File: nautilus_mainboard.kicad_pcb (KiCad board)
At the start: 4 copper layers, 176.2 x 177.5 mm, 83 parts, among them IC1 STM32H7B0RBT6, IC3 TPS2121RUXT, IC4 TPS2121RUXT, IC5 TPS2121RUXT, J18 179-UJ20CHC4SMTTR, J2 61300211121, J3 1761681-3, J4 Header male 1x05, J5 1792876, J7 LPHT-04-16-L-RT1-GP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

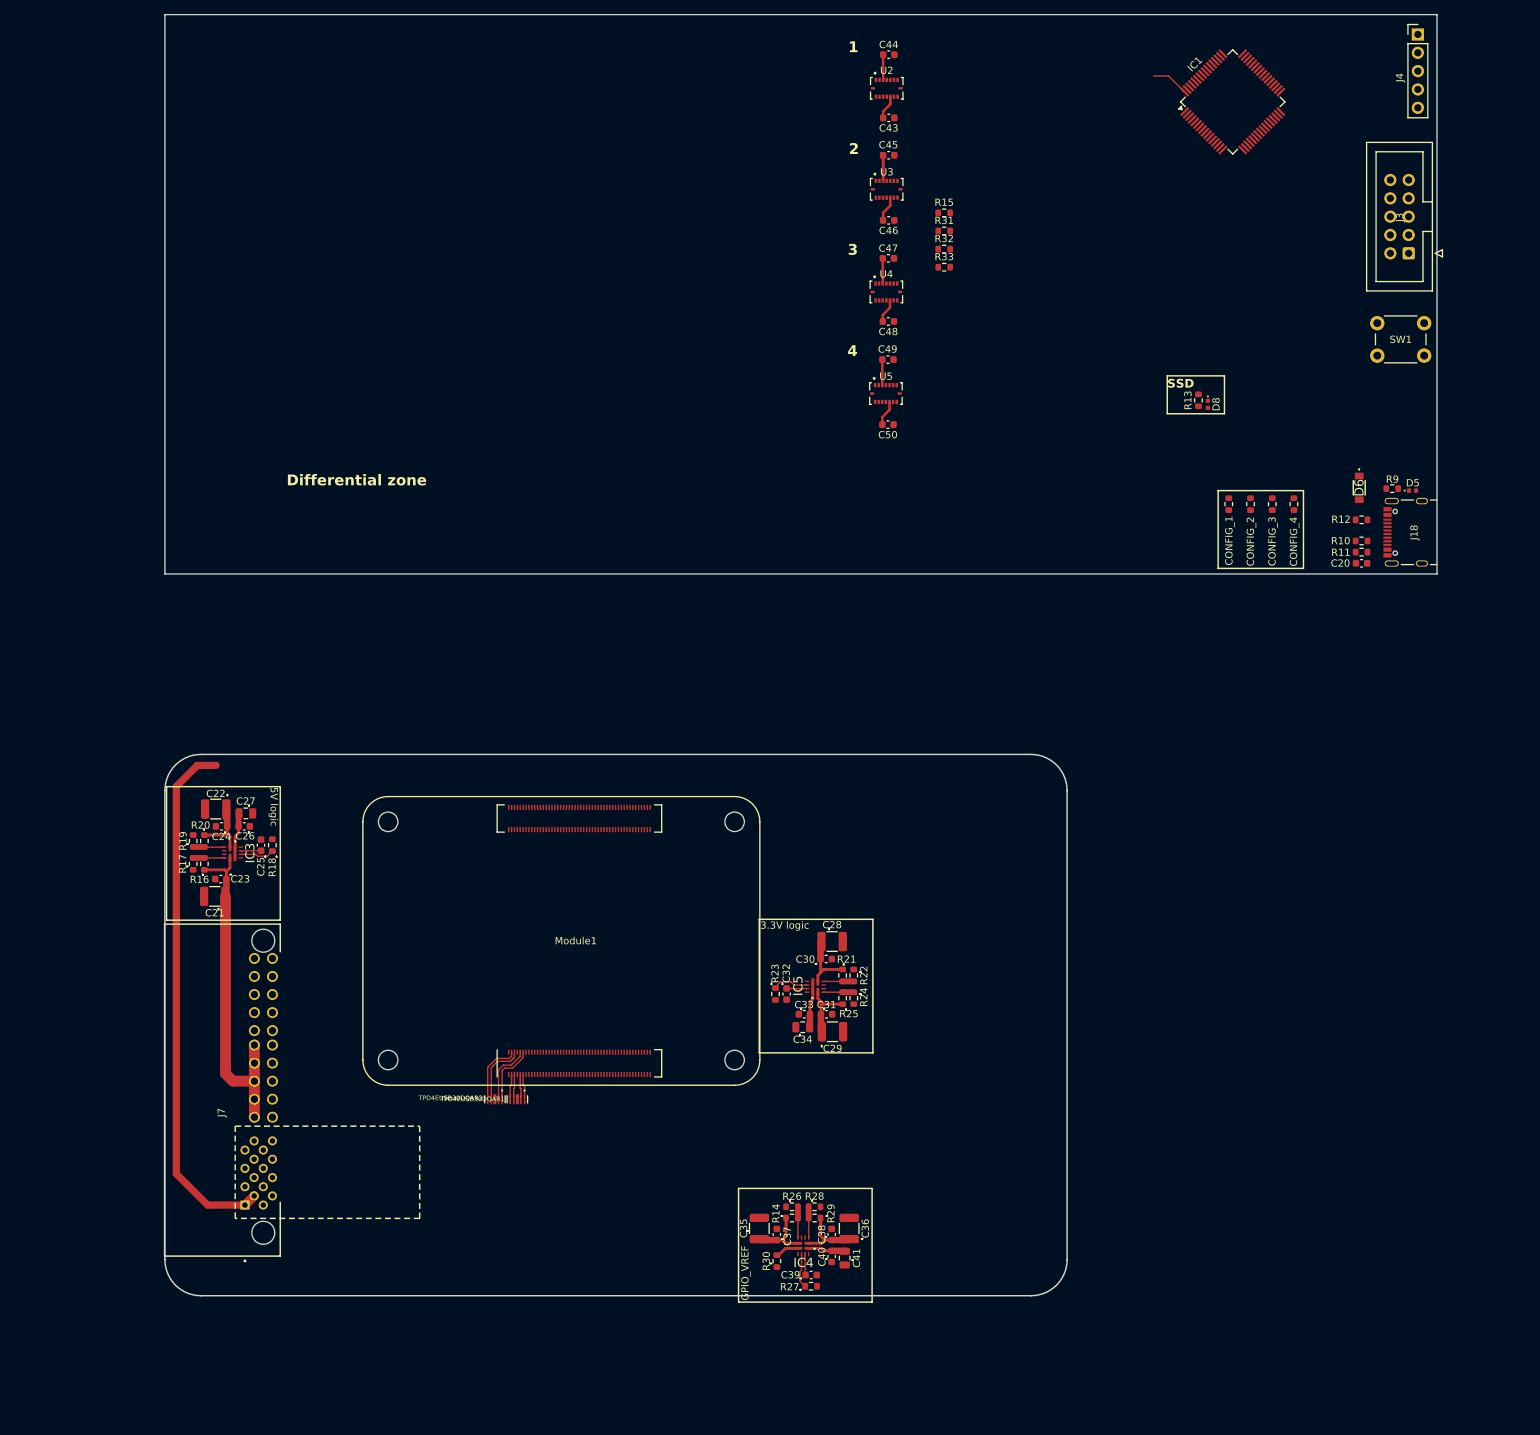
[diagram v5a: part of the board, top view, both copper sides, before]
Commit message: first tries with signal tracks
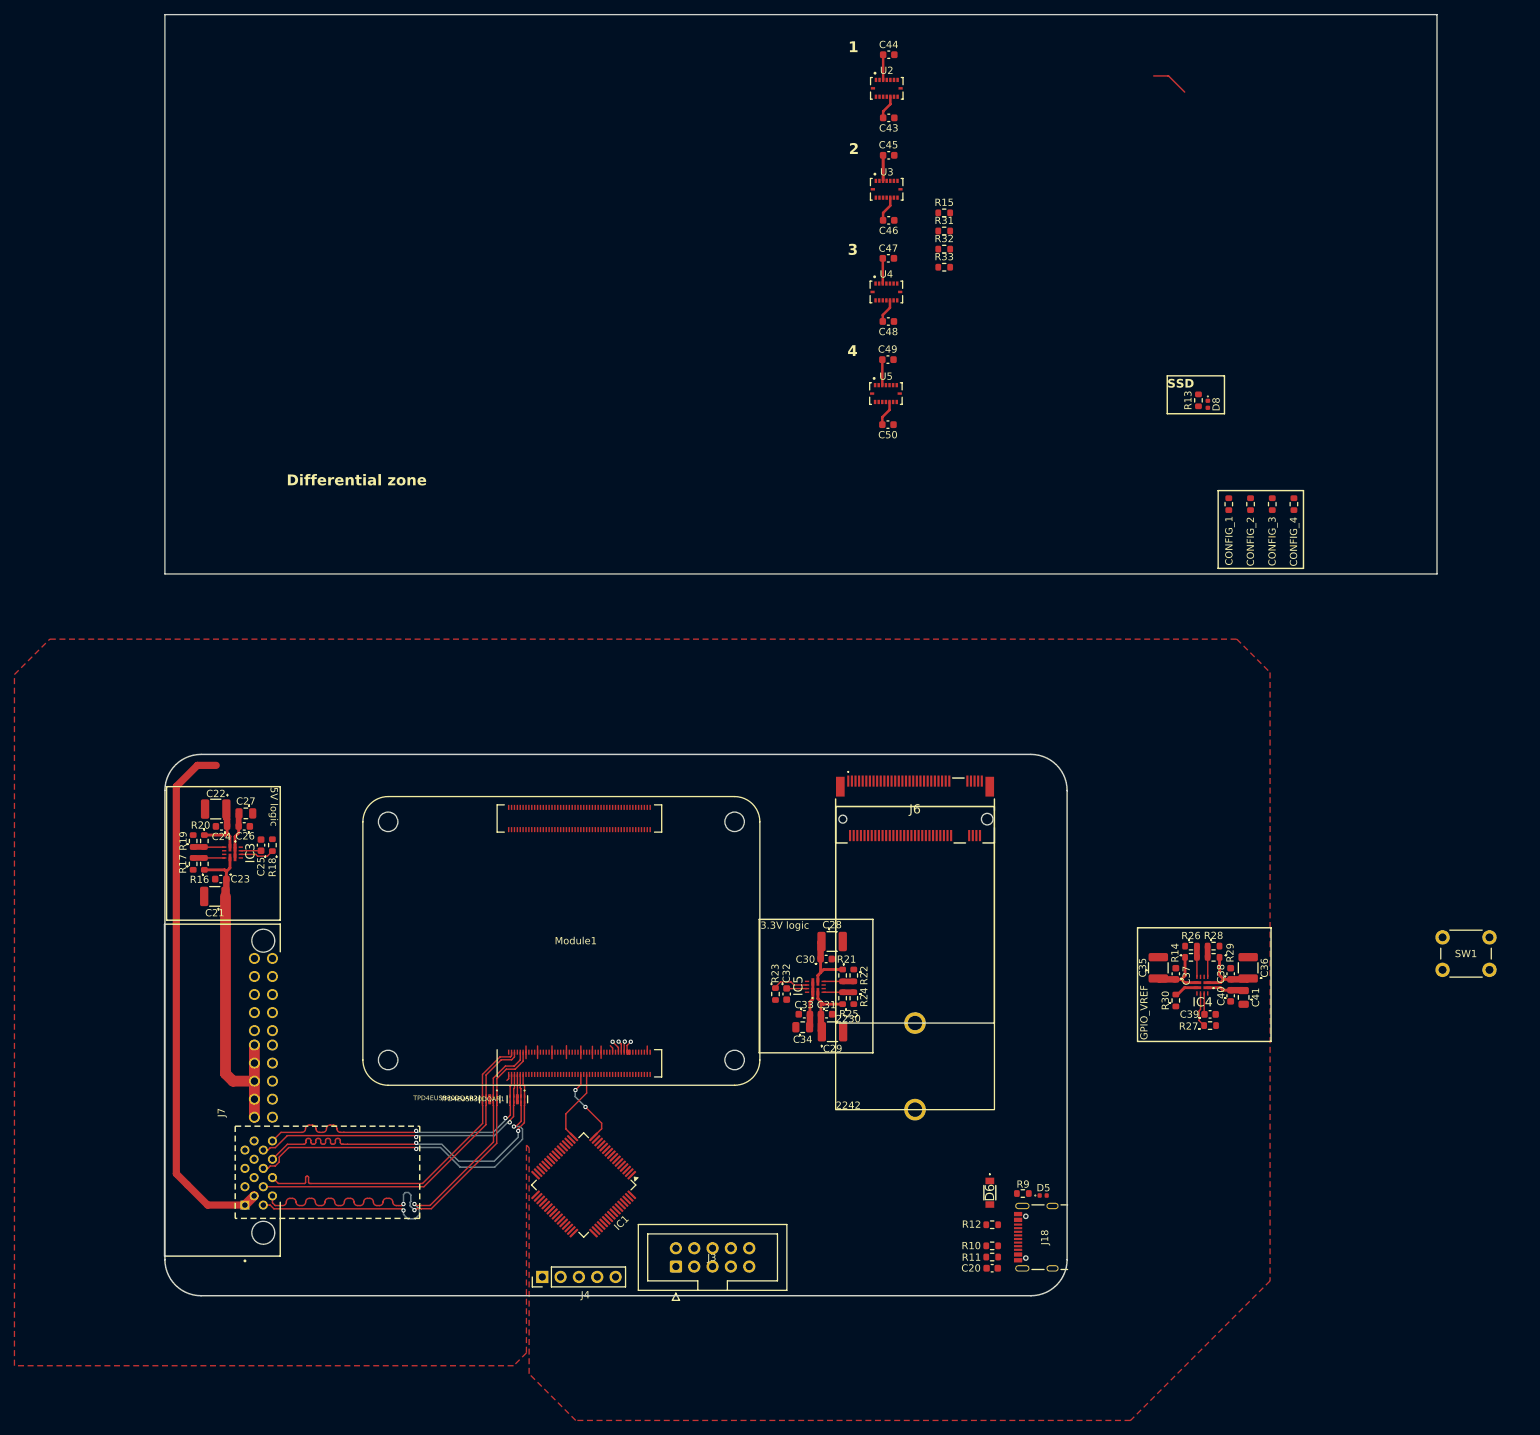
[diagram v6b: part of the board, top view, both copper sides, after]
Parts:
- added J6: MDT275M02001, dz_con:PCIE_MDT275M02001, F.Cu at (174.9, 157.8)
- moved J4 210.6 mm to (123.3, 222.4), turned to 90 degrees
- moved IC1 175.0 mm to (129.0, 209.7), turned to -135 degrees
- moved J3 173.2 mm to (141.8, 221.0), turned to 90 degrees
- moved D5 110.3 mm to (192.7, 211.1)
- moved R10 110.3 mm to (185.6, 218.1)
- moved R9 110.3 mm to (189.9, 210.8)
- moved C20 110.3 mm to (185.6, 221.2)
- moved D6 110.3 mm to (185.3, 210.7)
- moved J18 110.3 mm to (193.0, 216.9)
- moved R11 110.3 mm to (185.6, 219.6)
- moved R12 110.3 mm to (185.6, 215.2)
- moved SW1 85.6 mm to (248.0, 175.3)
- moved C35 66.0 mm to (208.6, 179.6)
- moved C36 66.0 mm to (221.1, 179.6)
- moved C40 66.0 mm to (218.7, 183.4)
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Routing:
- net /CM4/CM4_Module1A/TRD0_P: track 8.78 -> 61.0 mm, vias 0 -> 2
- net /CM4/CM4_Module1A/TRD2_N: track 3.90 -> 51.0 mm, vias 0 -> 2
- net /CM4/CM4_Module1A/TRD2_P: track 3.94 -> 50.9 mm, vias 0 -> 2
- net /CM4/CM4_Module1A/TRD0_N: track 8.83 -> 54.3 mm, vias 0 -> 2
- net /CM4/CM4_Module1A/TRD3_N: track 3.90 -> 42.8 mm, vias 0 -> 2
- net /CM4/CM4_Module1A/TRD3_P: track 3.94 -> 42.6 mm, vias 0 -> 2
- net /CM4/CM4_Module1A/TRD1_P: track 9.35 -> 47.0 mm
- net /CM4/CM4_Module1A/TRD1_N: track 9.52 -> 46.9 mm
- net GND: track 1.67 -> 19.7 mm
- net /CM4/CM4_Module1A/GPIO15: track 0.00 -> 11.0 mm, vias 0 -> 2
- net /CM4/CM4_Module1A/GPIO14: track 0.00 -> 10.3 mm
- net CM4_LED_IN_3.3V: track 9.20 -> 11.3 mm, vias 0 -> 1
- net GPIO_VREF_3.3V: track 8.61 -> 10.4 mm, vias 0 -> 1
- net /CM4/CM4_Module1A/SCL0: track 0.00 -> 1.66 mm, vias 0 -> 1
- net /CM4/CM4_Module1A/SDA0: track 0.00 -> 1.51 mm, vias 0 -> 1
- added copper zone on F.Cu, net GND
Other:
- board text added: "SORRY :("

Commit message: routed the CAN
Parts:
- added C1: 100nF, Capacitor_SMD:C_0603_1608Metric, F.Cu at (276.3, 66.9)
- added C10: 2.2pF, Capacitor_SMD:C_0402_1005Metric, F.Cu at (264.1, 75.9)
- added C11: 100nF, Capacitor_SMD:C_0603_1608Metric, F.Cu at (260.6, 66.9)
- added C12: 10pF, Capacitor_SMD:C_0603_1608Metric, F.Cu at (260.6, 69.4)
- added C13: 10pF, Capacitor_SMD:C_0603_1608Metric, F.Cu at (260.6, 71.9)
- added C14: 10pF, Capacitor_SMD:C_0603_1608Metric, F.Cu at (260.6, 74.4)
- added C15: 2.2pF, Capacitor_SMD:C_0402_1005Metric, F.Cu at (264.1, 77.8)
- added C16: 10pF, Capacitor_SMD:C_0603_1608Metric, F.Cu at (260.6, 76.9)
- added C17: 10pF, Capacitor_SMD:C_0603_1608Metric, F.Cu at (260.6, 79.4)
- added C18: 10pF, Capacitor_SMD:C_0603_1608Metric, F.Cu at (260.6, 81.9)
- added C19: 100nF, Capacitor_SMD:C_0603_1608Metric, F.Cu at (260.6, 84.5)
- added C2: 100nF, Capacitor_SMD:C_0603_1608Metric, F.Cu at (276.3, 69.4)
- added C3: 100nF, Capacitor_SMD:C_0603_1608Metric, F.Cu at (276.3, 71.9)
- added C4: 100nF, Capacitor_SMD:C_0603_1608Metric, F.Cu at (276.3, 74.4)
- added C42: 1uF, Capacitor_SMD:C_0603_1608Metric, F.Cu at (276.3, 84.5)
- added C5: 100nF, Capacitor_SMD:C_0603_1608Metric, F.Cu at (276.3, 76.9)
- added C6: 100nF, Capacitor_SMD:C_0603_1608Metric, F.Cu at (276.3, 79.4)
- added C7: 1uF, Capacitor_SMD:C_0603_1608Metric, F.Cu at (276.3, 81.9)
- added C8: 4.7pF, Capacitor_SMD:C_0402_1005Metric, F.Cu at (264.1, 71.9)
- added C9: 4.7pF, Capacitor_SMD:C_0402_1005Metric, F.Cu at (264.1, 73.9)
- added D1: APHHS1005LSECK/J3-PF, LED_SMD:LED_0402_1005Metric, F.Cu at (280.5, 88.7)
- added D2: APHHS1005LZGCK-V, LED_SMD:LED_0402_1005Metric, F.Cu at (263.9, 91.2)
- added D3: APHHS1005LSYCK/J3-PF, LED_SMD:LED_0402_1005Metric, F.Cu at (289.7, 88.7)
- added D4: APHHS1005LZGCK-V, LED_SMD:LED_0402_1005Metric, F.Cu at (289.7, 90.7)
- added IC2: TCAN3414DRBR, dz_comm:TCAN3414DRBR, F.Cu at (77.0, 212.0)
- added J1: 61300211121, dz_con:Wurth_Con_61300211121, F.Cu at (281.7, 67.8)
- added R1: 2.2k, Resistor_SMD:R_0603_1608Metric, F.Cu at (289.1, 73.6)
- added R2: 4.3k, Resistor_SMD:R_0603_1608Metric, F.Cu at (289.1, 76.1)
- added R5: 1k, Resistor_SMD:R_0603_1608Metric, F.Cu at (276.3, 92.7)
- added R6: 1k, Resistor_SMD:R_0603_1608Metric, F.Cu at (260.6, 89.0)
- added R7: 1k, Resistor_SMD:R_0603_1608Metric, F.Cu at (286.0, 89.0)
- added R8: 1k, Resistor_SMD:R_0603_1608Metric, F.Cu at (286.0, 91.5)
- added TP1: Test Point, TestPoint:TestPoint_Pad_D1.5mm, F.Cu at (280.1, 93.2)
- added TP2: Test Point, TestPoint:TestPoint_Pad_D1.5mm, F.Cu at (260.4, 92.0)
- added TPD4EUSB30DQAR3: ~, dz_con:IC_TPD4EUSB30DQAR, F.Cu at (288.9, 81.4)
- added U1: Buffers & Line Driver, dz_dio:SOT65P210X110-5N, F.Cu at (276.6, 89.6)
- added Y1: CC4V-T1A-32.768kHz-6pF-20PPM-TA-QC, dz_sens:CC4VT1A, F.Cu at (268.0, 68.3)
- moved SW1 111.6 mm to (142.2, 211.0), turned to 90 degrees
- moved C41 55.4 mm to (175.4, 215.9)
- moved C36 55.4 mm to (176.1, 211.8)
- moved C37 55.4 mm to (166.0, 212.7)
- moved C38 55.4 mm to (173.6, 212.7)
- moved C39 55.4 mm to (170.8, 218.3)
- moved C40 55.4 mm to (173.6, 215.7)
- moved IC4 55.4 mm to (169.7, 214.2)
- moved R27 55.4 mm to (170.8, 219.8)
- moved R30 55.4 mm to (166.0, 216.3)
- moved C35 55.4 mm to (163.6, 211.8)
- moved R14 55.4 mm to (168.1, 210.4)
- moved R26 55.4 mm to (168.1, 208.8)
- moved R28 55.4 mm to (171.3, 208.8)
- moved R29 55.4 mm to (171.3, 210.4)
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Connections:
- J7 pad 07: /LPHS-connector/CAN_H -> ST_CAN_P
- J7 pad 08: /LPHS-connector/CAN_L -> ST_CAN_N
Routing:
- net /STM/PinoutSTM/CAN1_RX: track 0.00 -> 59.1 mm, vias 0 -> 2
- net /STM/PinoutSTM/CAN1_TX: track 0.00 -> 56.9 mm
- net ST_CAN_N: track 0.00 -> 13.2 mm, vias 0 -> 2
- net ST_CAN_P: track 0.00 -> 13.2 mm, vias 0 -> 2
- net /STM/PinoutSTM/USART1_TX: track 0.00 -> 11.6 mm, vias 0 -> 1
- net /STM/PinoutSTM/USART1_RX: track 0.00 -> 10.9 mm, vias 0 -> 1
- net BMI_IN_3.3V: track 52.0 -> 46.8 mm
- net Battery_Out_3.3V: track 82.5 -> 87.3 mm, vias 0 -> 1

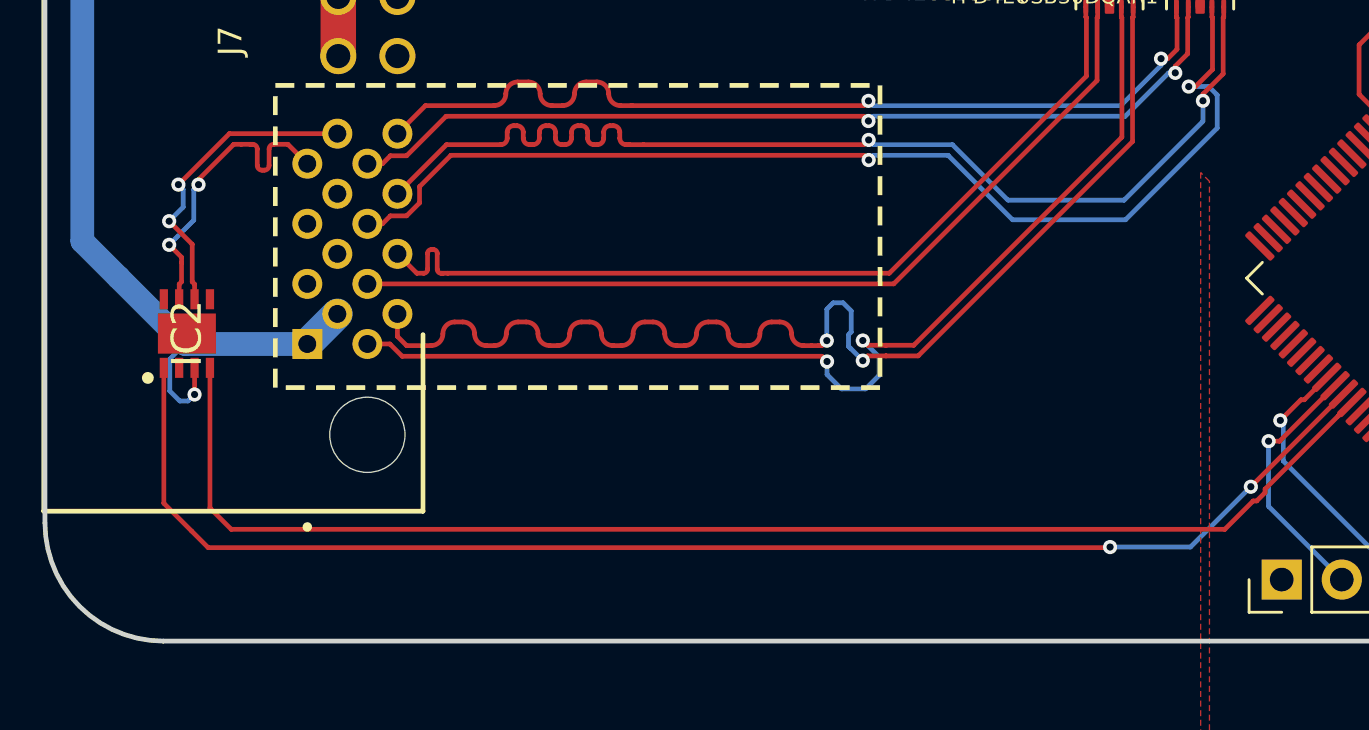
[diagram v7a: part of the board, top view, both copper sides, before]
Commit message: fixed the can tranciever placement
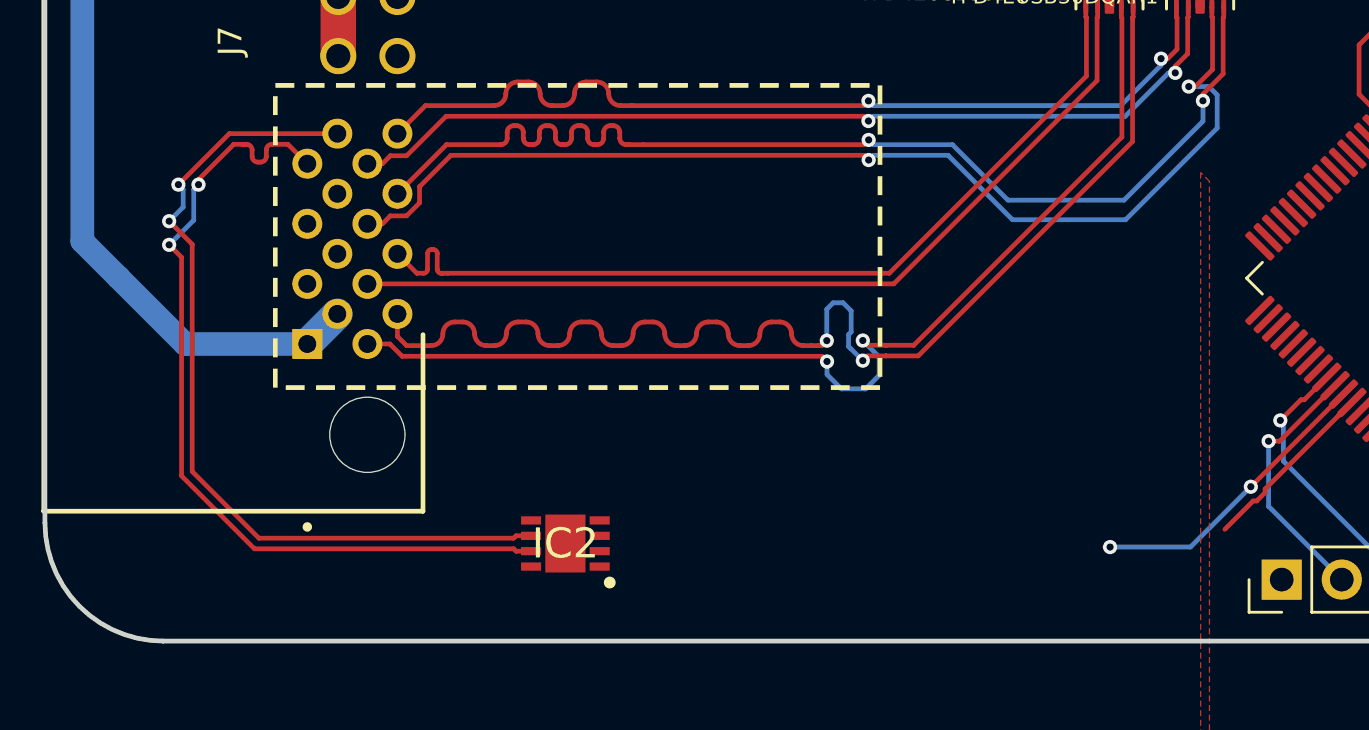
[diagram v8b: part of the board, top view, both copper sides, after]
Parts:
- moved IC2 18.3 mm to (93.0, 220.9), turned to 180 degrees
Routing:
- net /STM/PinoutSTM/CAN1_TX: track 56.9 -> 7.68 mm
- net /STM/PinoutSTM/CAN1_RX: track 59.1 -> 12.8 mm
- net ST_CAN_N: track 13.2 -> 36.0 mm
- net ST_CAN_P: track 13.2 -> 36.0 mm
- net Battery_Out_3.3V: track 87.3 -> 82.5 mm, vias 1 -> 0
